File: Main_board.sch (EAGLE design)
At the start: 56 parts, among them IC1 4050D, U1 MCP73831, U2 TPS61200, U3 MAX1704X, U4 USD-SOCKETNEW, X1 USB-MICROB, Y1 16MHz KX-7

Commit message: Big update
Replacement of old file by only one unique file
Reorganisation of schematics
Integration of the screen footprint
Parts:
- removed HMC8339: (no value), SparkFun:M04PTH
- removed SJ2: UVLO Disable, SparkFun-Passives:SOLDERJUMPERNO
- added C19: 1µ, SparkFun-Passives:CAP0805
- added C20: 0.1µ, SparkFun-Passives:CAP0805
- added C21: 10µ, SparkFun-Passives:CAP0805
- added C22: 22uF, SparkFun:CAP0805
- added C23, C24: 0.1uF, SparkFun:CAP0805
- added C25: 10uF, SparkFun:CAP0805
- added D1: (no value), SparkFun-DiscreteSemi:DIODEHV
- added FER: (no value), dp_devices:FERRITE-1206
- added HMC5883: (no value), SparkFun:M04PTH
- added L3: 4.7uH, 1.2A, SparkFun:INDUCTOR.
- added Q1: (no value), SparkFun-DiscreteSemi:IRF7509
- added R16: 10k, SparkFun-Passives:RESISTOR0805-RES
- added R17, R19: 100k, SparkFun-Passives:RESISTOR0805-RES
- added R18: 300k, SparkFun-Passives:RESISTOR0805-RES
- added R20: 2M, SparkFun:RESISTOR0805-RES
- added R21: 220k, SparkFun:RESISTOR0805-RES
- added S1: SWITCH-MOMENTARY-2SMD, SparkFun-Electromechanical:SWITCH-MOMENTARY-2SMD
- added U5: TPS61200, SparkFun:TPS61200
- R11: value 10k -> 2M
- R12: value 10k -> 220k
- U$2: value (none) -> µLCD-32PT; device dp_devices:FERRITE-1206 -> 4DSystems:µLCD-32PT
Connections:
- removed net EN: R11.2, U2.EN
- removed net PS: R12.2, U2.PS
- removed net VBATT: C10.1, C11.1, C16.1, JP2.2, L2.2, R11.1, R12.1, R3.2, SJ2.2, U1.VBAT, U2.VIN
- new net 5V: C22.1, R20.2, U$2.J2-P6, U5.VOUT
- new net EN5V: U5.EN
- new net IOPIN: D1.A, R18.1, R19.1
- new net N$15: C21.1, Q1NMOS.G, R18.2
- new net N$16: L3.1, U5.L
- new net N$17: C24.1, U5.VAUX
- new net N$18: C19.1, D1.C, R16.1, S1.2
- new net N$20: C19.2, C20.1, Q1NMOS.S, Q1PMOS.G, R17.1
- new net UVLO1: C23.2, R11.1, R12.2, U5.UVLO
- new net VIN: C11.1, C16.1, C21.2, C23.1, C25.1, L2.2, L3.2, Q1PMOS.S, R11.2, R19.2, R3.2, U2.EN, U2.PS, U2.VIN, U5.PS, U5.VIN
- new net V_BATT: C10.1, C20.2, JP2.2, Q1PMOS.D, R14.2, R15.2, R16.2, R17.2, U1.VBAT
- net AUX_SCL: now also HMC5883.4
- net AUX_SDA: now also HMC5883.3
- net FB: now also R20.1, R21.2, U5.FB
- net GND: now also C22.2, C24.2, C25.2, HMC5883.1, Q1NMOS.D, S1.1, U$2.J1-P15, U$2.J2-P15, U$2.J2-P17, U5.PAD@1, U5.PAD@2, U5.PAD@3, U5.PAD@4, U5.PAD@5, U5.PGND; no longer HMC8339.1
- net GND1: now also R12.1, R21.1, U5.GND
- net N$9: now also FER.2; no longer U$2.2
- net RX: now also U$2.J2-P27
- net SCL: no longer HMC8339.4
- net SDA: no longer HMC8339.3
- net TX: now also U$2.J2-P29
- net UVLO: no longer SJ2.1
- net VCC: now also FER.1, HMC5883.2, U$2.J1-P18, U$2.J2-P16, U$2.J2-P18; no longer HMC8339.2, R14.2, R15.2, U$2.1
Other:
- note added: "Battery Level Measurement"
- note added: "Sensors"
- note added: "Switching Regulator 3.3V"
- note added: "Switching Regulator 5V"
- note added: "Turn on/off control"
- note added: "µC"
- note added: "µSD Card"
- note removed: "*close jumper SJ2 to disable UVLO*"
- note removed: "Switching Regulator"
- moved on the sheet: ATMEGA, C1, C10, C11, C12, C13, C14, C15, C16, C17, C18, C2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

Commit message: Final design
Board routed and schematics finalised and cleaned
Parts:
- removed C23: 0.1uF, SparkFun:CAP0805
- removed C25: 10uF, SparkFun:CAP0805
- removed HMC5883, TMP102: (no value), SparkFun:M04PTH
- removed MPU-6050: M10", SparkFun:M10"
- removed R11: 2M, SparkFun:RESISTOR0805-RES
- removed R12: 220k, SparkFun:RESISTOR0805-RES
- added U$6: HMC5883, SparkFun-Breakouts:HMC5883
- added U$7: MPU-6050, SparkFun-Breakouts:MPU-6050
- added U$8: TMP102, SparkFun-Breakouts:TMP102
- D1: device SparkFun-DiscreteSemi:DIODEHV -> SparkFun-DiscreteSemi:DIODESMA-ALT
- S1: value SWITCH-MOMENTARY-2SMD -> (none); device SparkFun-Electromechanical:SWITCH-MOMENTARY-2SMD -> SparkFun-Electromechanical:TAC_SWITCHSMD
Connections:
- removed net +3V3: IC1P.VDD, U4.VCC
- removed net EN5V: U5.EN
- removed net IOPIN: D1.A, R18.1, R19.1
- removed net UVLO1: C23.2, R11.1, R12.2, U5.UVLO
- net A5: now also U5.EN
- net AUX_SCL: now also U$6.SCL, U$7.AUX_SCL; no longer HMC5883.4, MPU-6050.2
- net AUX_SDA: now also U$6.SDA, U$7.AUX_SDA; no longer HMC5883.3, MPU-6050.1
- net CLKIN: now also U$7.CLKIN; no longer MPU-6050.3
- net D7: now also D1.A, R18.1, R19.1
- net FSYNC: now also U$7.FSYNC; no longer MPU-6050.7
- net GND: now also S1.2, U$6.GND, U$7.GND, U$8.ADD0, U$8.GND; no longer C25.2, HMC5883.1, MPU-6050.9, TMP102.4
- net GND1: no longer R12.1
- net INT: now also U$7.INT; no longer MPU-6050.8
- net IO10*: now also IC1A.I; no longer IC1C.I
- net IO13*: now also IC1C.I; no longer IC1A.I
- net N$12: now also IC1C.O; no longer IC1A.O
- net N$13: now also IC1A.O; no longer IC1C.O
- net N$18: now also S1.3, S1.4; no longer S1.2
- net SCL: now also U$7.SCL, U$8.SCL; no longer MPU-6050.6, TMP102.3
- net SDA: now also U$7.SDA, U$8.SDA; no longer MPU-6050.5, TMP102.2
- net VCC: now also IC1P.VDD, U$6.VCC, U$7.VCC, U$8.V+, U4.VCC; no longer HMC5883.2, MPU-6050.10, TMP102.1
- net VIN: now also U5.UVLO; no longer C23.1, C25.1, R11.2
- net VIO: now also U$7.VIO; no longer MPU-6050.4
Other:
- note added: "Screen"
- moved on the sheet: ATMEGA, C1, C10, C11, C12, C13, C14, C15, C16, C17, C18, C19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

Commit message: Board clean up
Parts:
- renumbered IC1 to 4050D, U1 to MCP73831

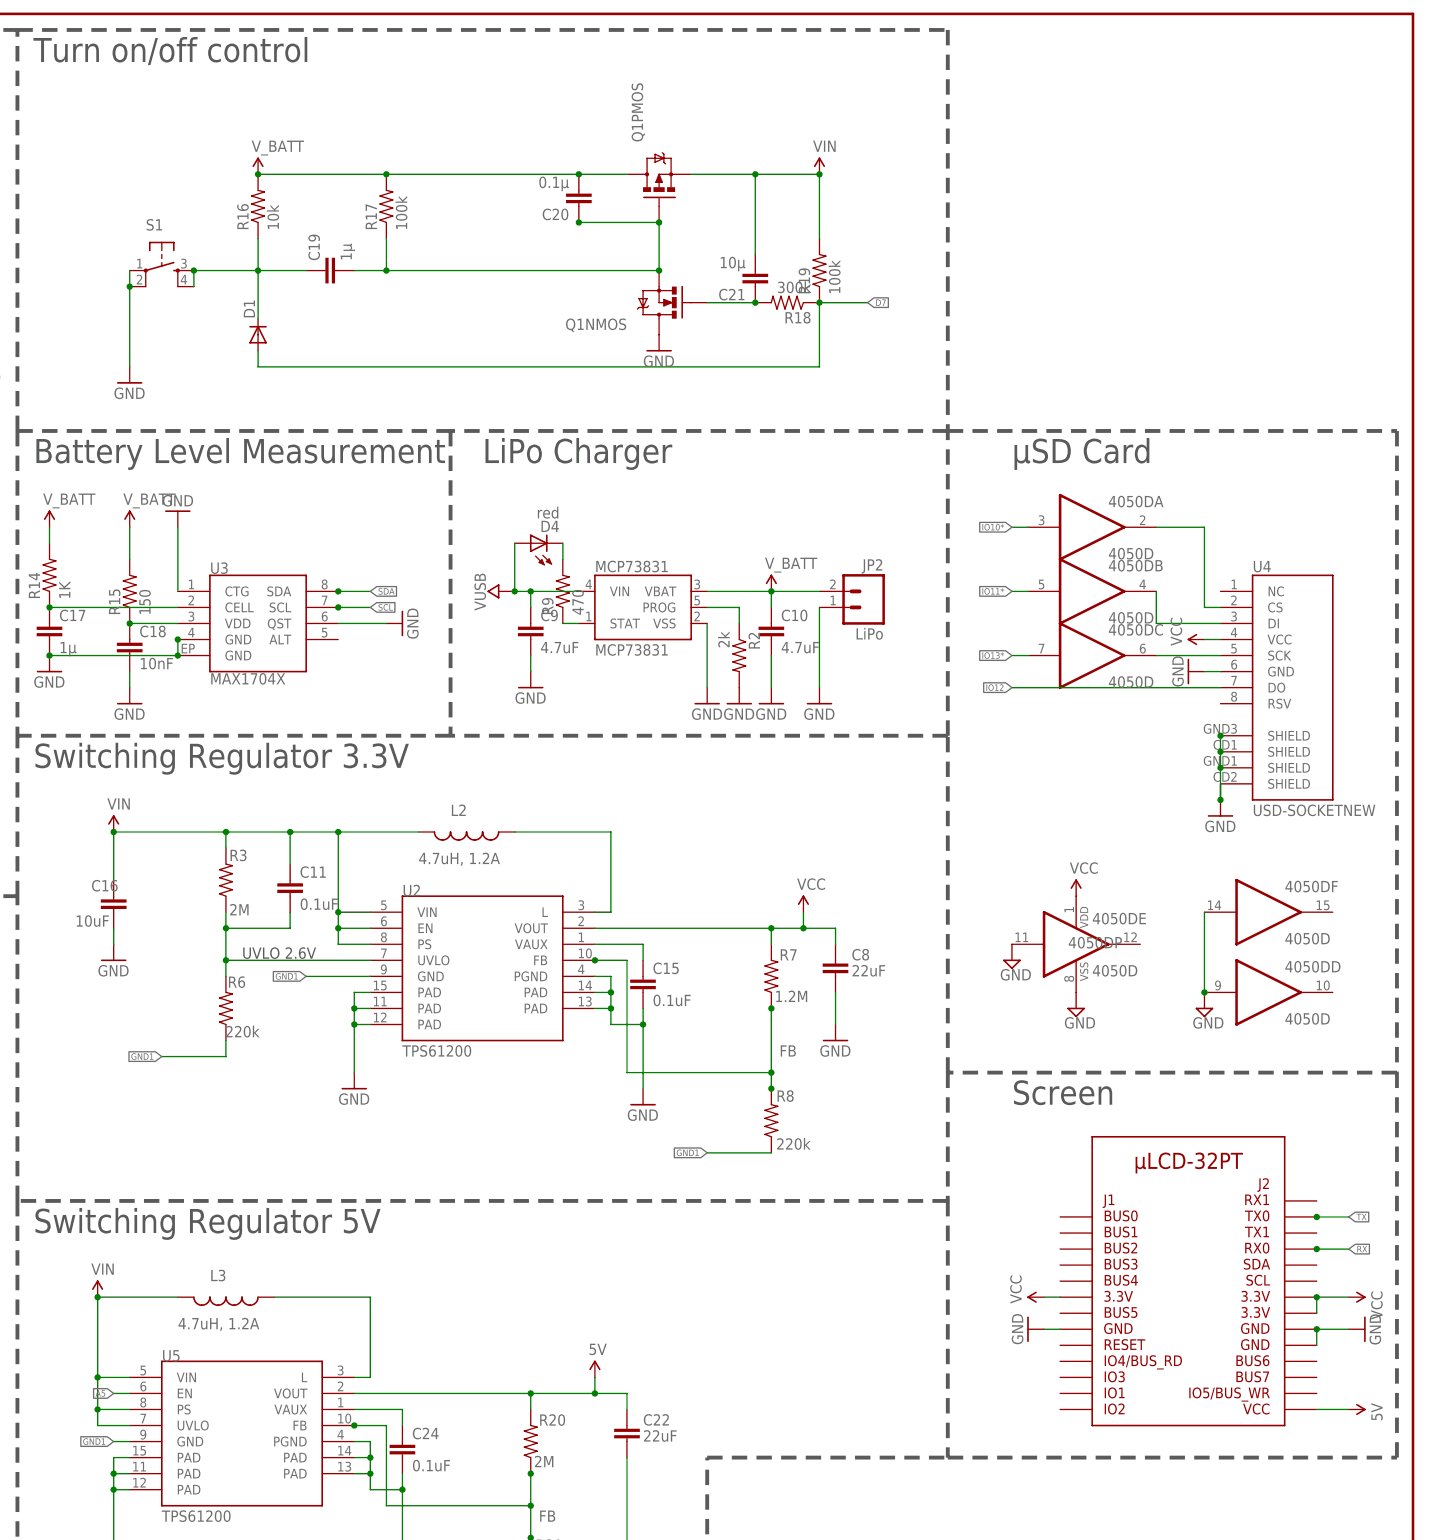
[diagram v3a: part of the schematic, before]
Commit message: Maxim library update + ON/OFF switch mod
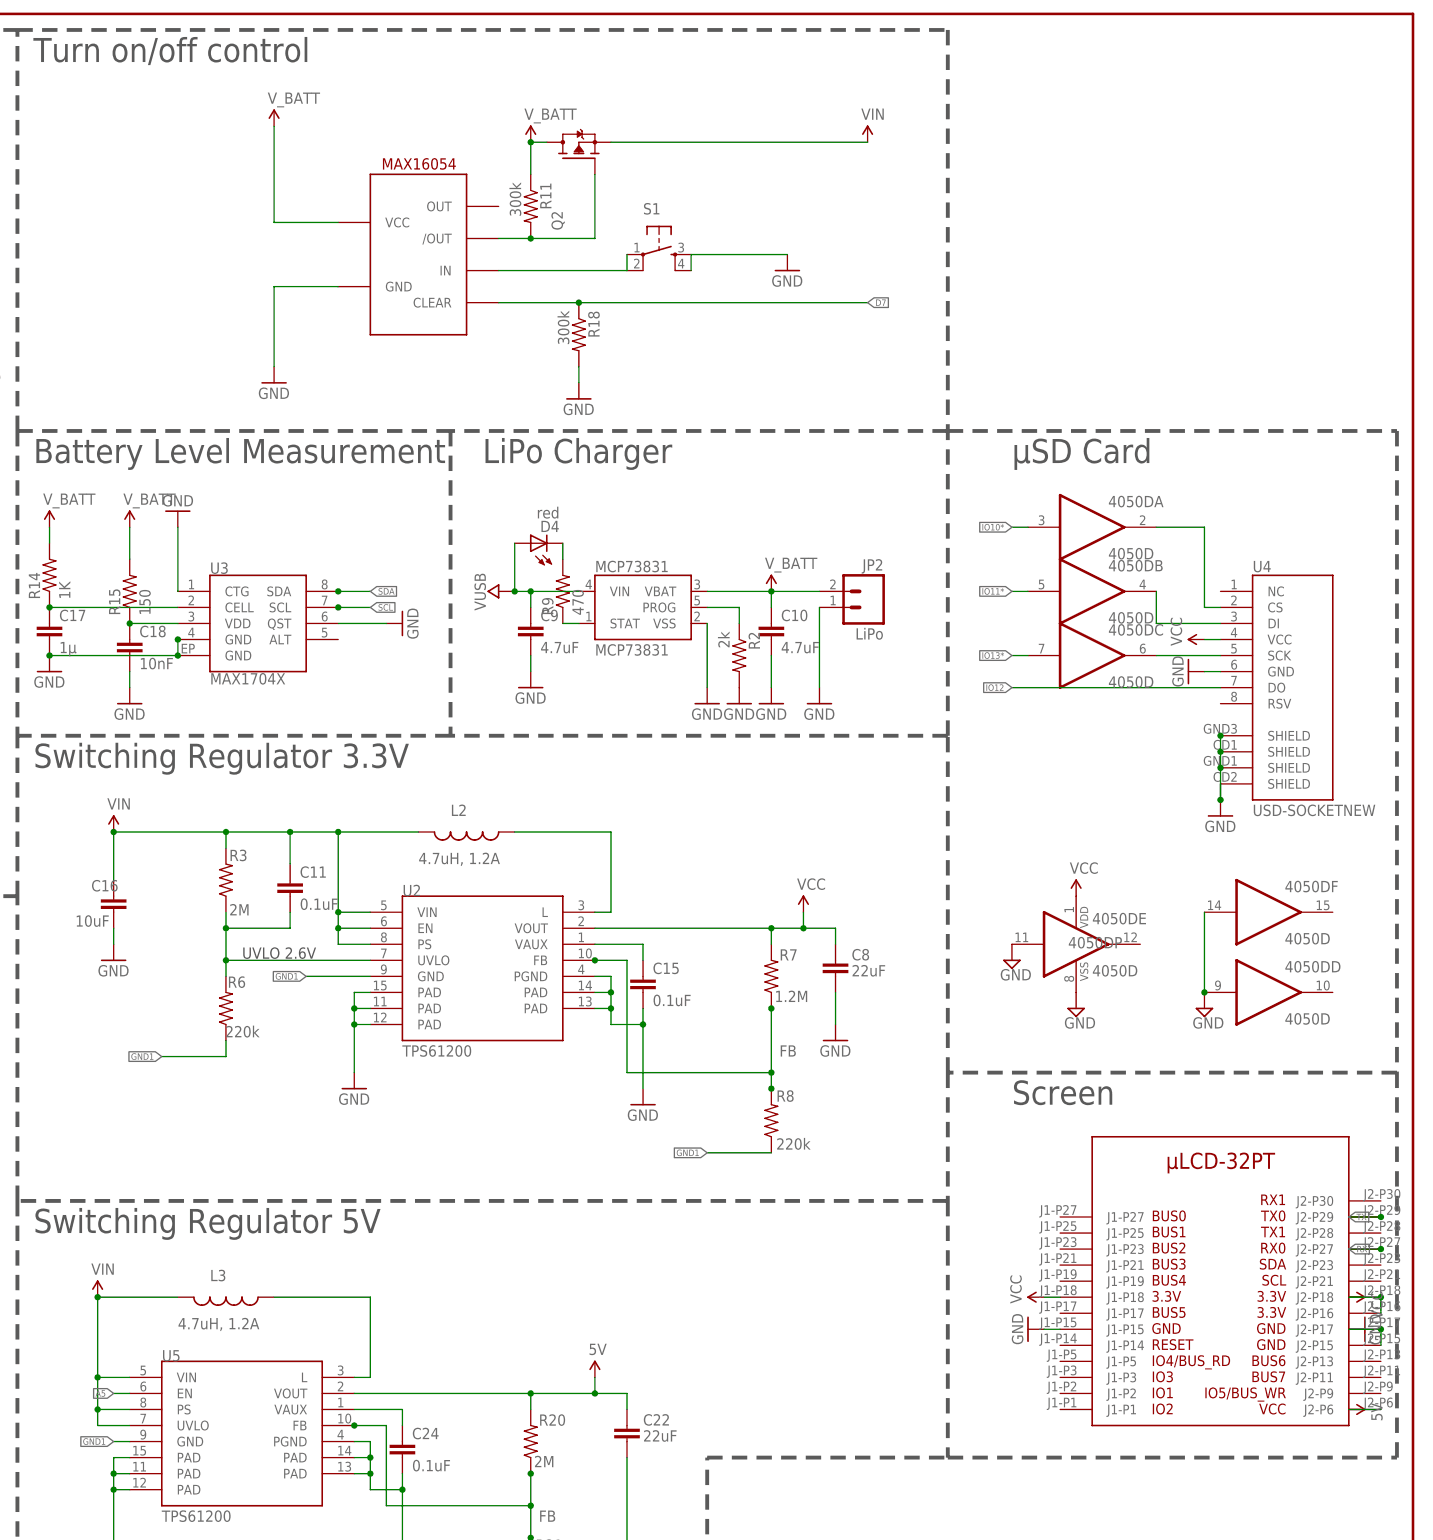
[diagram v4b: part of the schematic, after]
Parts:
- removed C19: 1µ, SparkFun-Passives:CAP0805
- removed C20: 0.1µ, SparkFun-Passives:CAP0805
- removed C21: 10µ, SparkFun-Passives:CAP0805
- removed D1: (no value), SparkFun-DiscreteSemi:DIODESMA-ALT
- removed Q1: (no value), SparkFun-DiscreteSemi:IRF7509
- removed R16: 10k, SparkFun-Passives:RESISTOR0805-RES
- removed R17, R19: 100k, SparkFun-Passives:RESISTOR0805-RES
- added Q2: (no value), dp_devices:TRANSISTOR_FET_TSM2301CX
- added R11: 300k, SparkFun-Passives:RESISTOR0805-RES
- added U$9: MAX16054, maxim:MAX16054
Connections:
- removed net N$18: C19.1, D1.C, R16.1, S1.3, S1.4
- removed net N$20: C19.2, C20.1, Q1NMOS.S, Q1PMOS.G, R17.1
- new net N$19: Q2.G, R11.2, U$9./OUT
- net D7: now also U$9.CLEAR; no longer D1.A, R19.1
- net GND: now also R18.2, S1.3, S1.4, U$9.GND; no longer Q1NMOS.D, S1.1, S1.2
- net N$15: now also S1.1, S1.2, U$9.IN; no longer C21.1, Q1NMOS.G, R18.2
- net VIN: now also Q2.S; no longer C21.2, Q1PMOS.S, R19.2
- net V_BATT: now also Q2.D, R11.1; no longer C20.2, Q1PMOS.D, R16.2, R17.2
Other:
- moved on the sheet: R18, S1
